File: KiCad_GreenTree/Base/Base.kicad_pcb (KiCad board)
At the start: 2 copper layers, 65 x 62.2 mm, 46 parts, among them Q1 BCX56, Q2 BCX56, Q3 BCX56, Q4 BCX56, SW1 SW_DPDT_x2, U1 NE555D, U2 NE555D, U3 74HC04, U4 L78L05_TO92

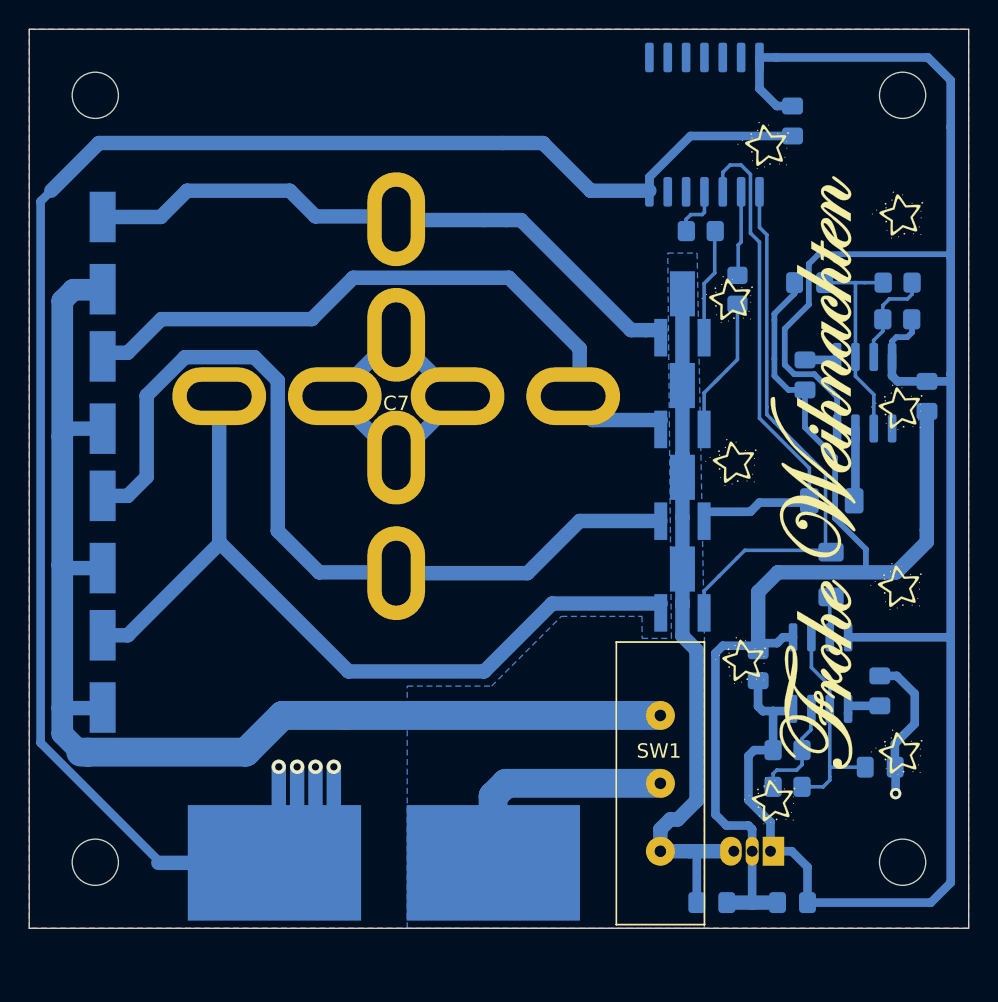
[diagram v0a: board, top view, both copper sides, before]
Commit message: nothing works
Transistoren gegen GND schalten
Footprint Inverter und Schalter ändern
Inverter Spannungslevel anpassen. (Schalten der Transistoren beachten)
SMD linearregler?
Größere Widerstande bestellen
Andere Füße
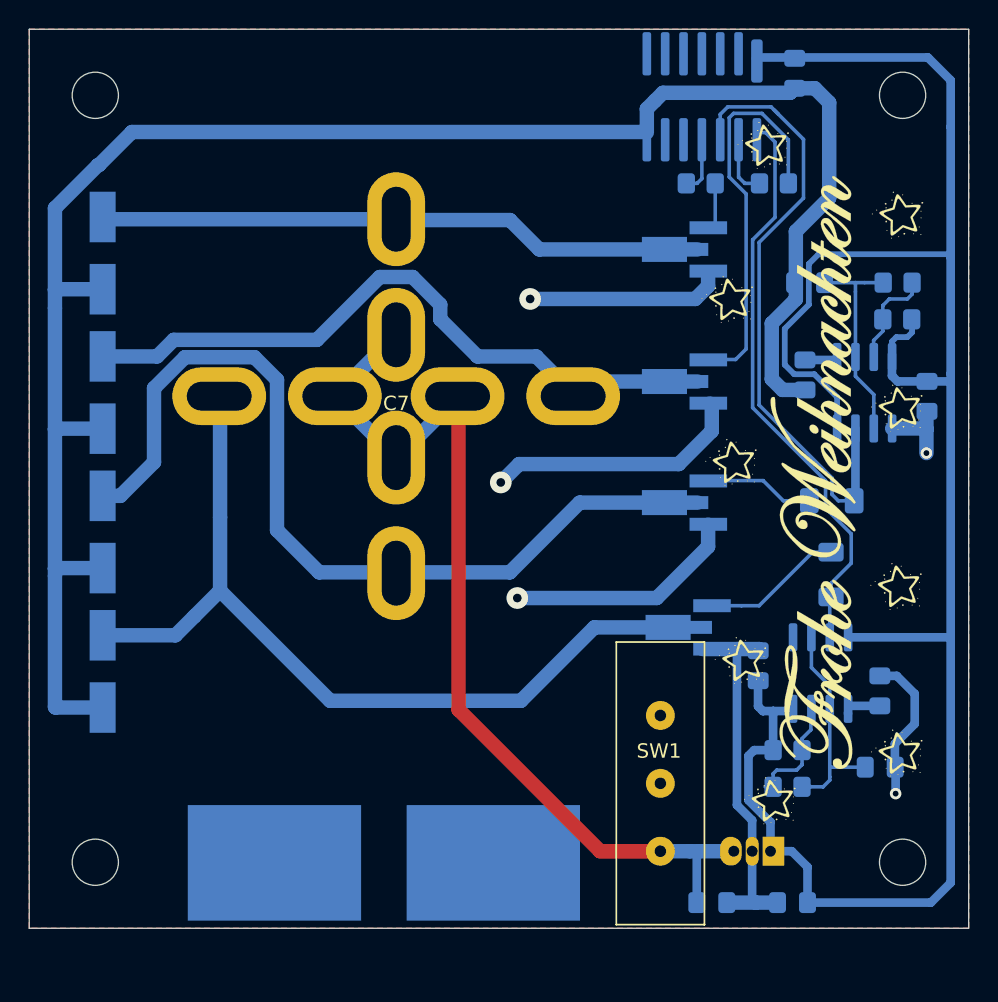
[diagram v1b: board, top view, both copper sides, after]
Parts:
- U3: footprint Package_SO:SOIC-14W_7.5x9mm_P1.27mm -> Package_SO:SOIC-14_3.9x8.7mm_P1.27mm
- moved R8 7.79 mm to (163.3, 77.7), turned to 180 degrees
- moved Q4 3.84 mm to (156.4, 82.3), turned to 180 degrees
- moved Q1 3.31 mm to (156.7, 108.4), turned to 180 degrees
- moved C8 3.31 mm to (164.7, 70.1)
- moved R7 3.30 mm to (158.2, 77.7)
- moved U3 1.94 mm to (158.3, 71.7)
- moved Q2 1.14 mm to (156.4, 99.8), turned to 180 degrees
- moved Q3 1.14 mm to (156.4, 91.4), turned to 180 degrees
- turned D1 to 90 degrees
- turned D2 to 90 degrees
- turned D3 to 90 degrees
- turned D4 to 90 degrees
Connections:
- C7 pad 1: GND -> VCC
- C7 pad 3: GND -> VCC
- C7 pad 5: GND -> VCC
- C7 pad 7: GND -> VCC
- D1 pad 1: /LED_MATRIX_4 -> GND
- D1 pad 2: +9V -> /LED_MATRIX_4
- D2 pad 1: /LED_MATRIX_3 -> GND
- D2 pad 2: +9V -> /LED_MATRIX_3
- D3 pad 1: /LED_MATRIX_2 -> GND
- D3 pad 2: +9V -> /LED_MATRIX_2
- D4 pad 1: /LED_MATRIX_1 -> GND
- D4 pad 2: +9V -> /LED_MATRIX_1
- Q1 pad 2: VCC -> /LED_MATRIX_1
- Q1 pad 3: /LED_MATRIX_1 -> GND
- Q2 pad 2: VCC -> /LED_MATRIX_2
- Q2 pad 3: /LED_MATRIX_2 -> GND
- Q3 pad 2: VCC -> /LED_MATRIX_3
- Q3 pad 3: /LED_MATRIX_3 -> GND
- Q4 pad 2: VCC -> /LED_MATRIX_4
- Q4 pad 3: /LED_MATRIX_4 -> GND
- U3 pad 1: Net-(Q1-Pad1) -> Net-(R6-Pad2)
- U3 pad 3: Net-(Q2-Pad1) -> Net-(R5-Pad2)
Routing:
- net +9V: track 85.1 -> 0.00 mm
- net Net-(R5-Pad2): track 5.21 -> 43.4 mm
- net Net-(R6-Pad2): track 2.73 -> 40.1 mm
- net Net-(Q2-Pad1): track 35.7 -> 7.84 mm
- net Net-(Q1-Pad1): track 38.0 -> 10.4 mm
- net GND: track 248.7 -> 222.7 mm
- net Net-(Q3-Pad1): track 8.78 -> 27.7 mm
- net VCC: track 48.8 -> 66.7 mm
- net Net-(BT3-Pad1): track 16.6 -> 0.00 mm
- net +5V: track 147.6 -> 143.0 mm
- net Net-(Q4-Pad1): track 7.03 -> 3.18 mm
- net /LED_MATRIX_2: track 59.8 -> 62.3 mm
- net /LED_MATRIX_1: track 57.4 -> 59.9 mm
- net /LED_MATRIX_4: track 44.5 -> 43.1 mm
- net Net-(R7-Pad2): track 3.68 -> 4.33 mm
- removed copper zone on B.Cu, net VCC
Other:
- board text added: "Designed by Tobi and Kai in Karlsruhe V 2.0"
- board text removed: "Designed by Tobi and Kai in Karlsruhe"

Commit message: Base V2.0
Finished Rework. Sould now work. Hoping for the best
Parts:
- moved SW1 3.30 mm to (158.5, 112.7)
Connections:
- BT3 pad 1: Net-(BT3-Pad1) -> VCC
- BT3 pad 2: GND -> Net-(BT3-Pad2)
- D1 pad 1: GND -> GND2
- D2 pad 1: GND -> GND2
- D3 pad 1: GND -> GND2
- D4 pad 1: GND -> GND2
- SW1 pad 1: VCC -> GND
- SW1 pad 2: Net-(BT3-Pad1) -> Net-(BT3-Pad2)
- SW1 pad 3: +9V -> GND2
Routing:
- net GND2: track 0.00 -> 80.3 mm
- net GND: track 222.7 -> 142.7 mm, vias 5 -> 6
- net Net-(BT3-Pad2): track 0.00 -> 40.3 mm
- net VCC: track 66.7 -> 91.7 mm, vias 0 -> 4
- net /LED_MATRIX_1: track 59.9 -> 57.0 mm
- added copper zone on B.Cu, net Net-(BT3-Pad2)
- added copper zone on B.Cu, net VCC

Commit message: V 2.0
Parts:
- moved C4 0.77 mm to (165.7, 83.8)
- moved R4 0.77 mm to (171.8, 83.8)
- moved R3 0.52 mm to (171.8, 86.6)
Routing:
- net Net-(C4-Pad1): track 13.6 -> 15.7 mm
- net +5V: track 143.0 -> 144.0 mm
- net Net-(R3-Pad2): track 7.32 -> 7.99 mm
